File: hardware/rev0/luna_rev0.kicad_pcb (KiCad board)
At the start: 4 copper layers, 56 x 56 mm, 313 parts, among them IC1 ECP5-BGA256, J1 USB_C_Receptacle_USB2.0, J10 TC_SWD, J2 USB_C_Receptacle_USB2.0, J3 USB_A, J4 USB_C_Receptacle_USB2.0, J5 MEZZANINE, J6 MCU_SWD, J7 PMOD_A, J8 PMOD_B, Q1 PMOS, Q10 2PNP, Q11 2NPN, Q12 PMOS, Q13 2PNP, Q14 2PNP, Q15 2PNP, Q2 PMOS, Q3 2NPN, Q4 PMOS, Q5 PMOS, Q6 PMOS, Q7 PMOS, Q8 2NPN, Q9 PMOS, SW1 BTN_PROGRAM, SW2 BTN_RESET, SW3 BTN_USER, U1 PAC195X-1-WLCSP, U10 HyperRAM, U11 USB3343-CP, U12 FUSB302BMPX, U13 DPO2036, U14 DPO2036, U15 MIC5504-1.8YM5, U16 PI3USB102G, U2 FUSB302BMPX, U3 AP7361EA-33, U4 TCR2EF115, U5 MIC5504-2.5YM5, U6 ATSAMD11, U7 W25Q32JVSS, U8 USB3343-CP, U9 USB3343-CP, Y1 Osc60MHz

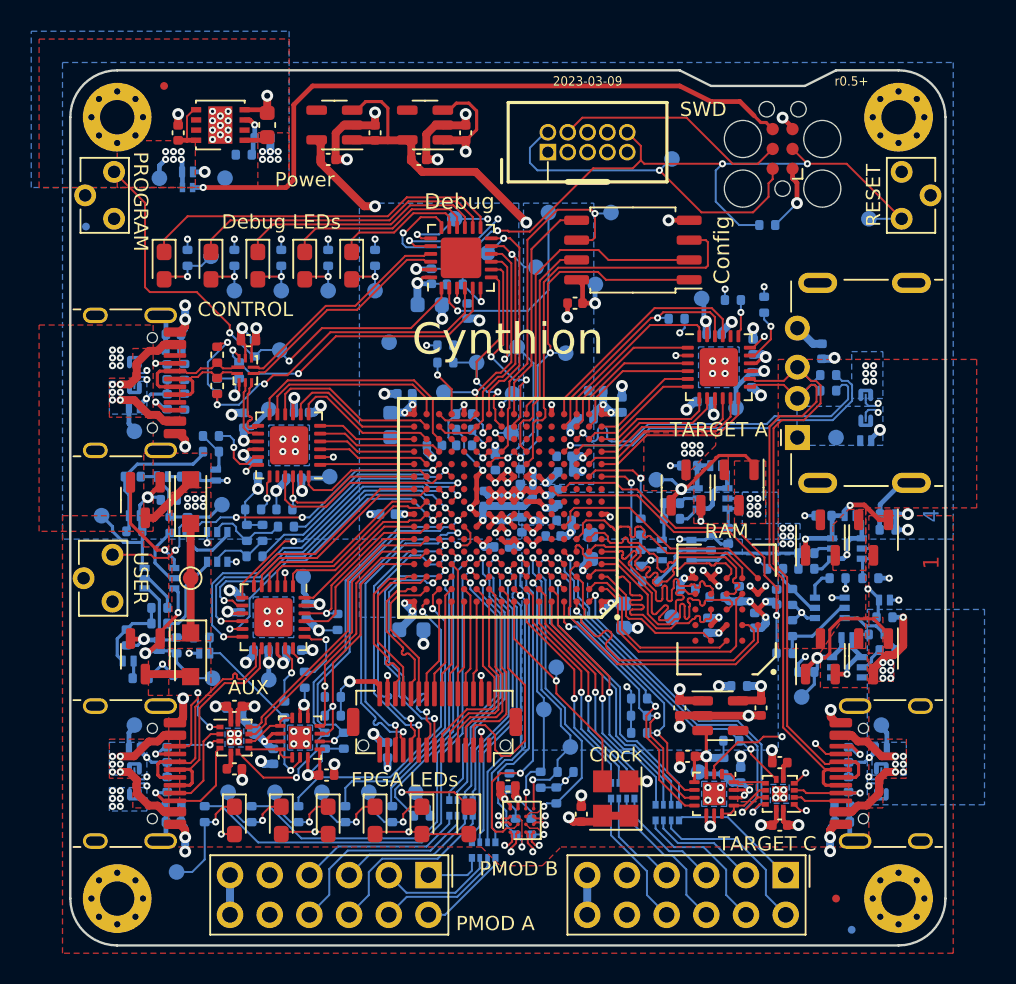
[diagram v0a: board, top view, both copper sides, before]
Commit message: Add additional silkscreen markings to front side.
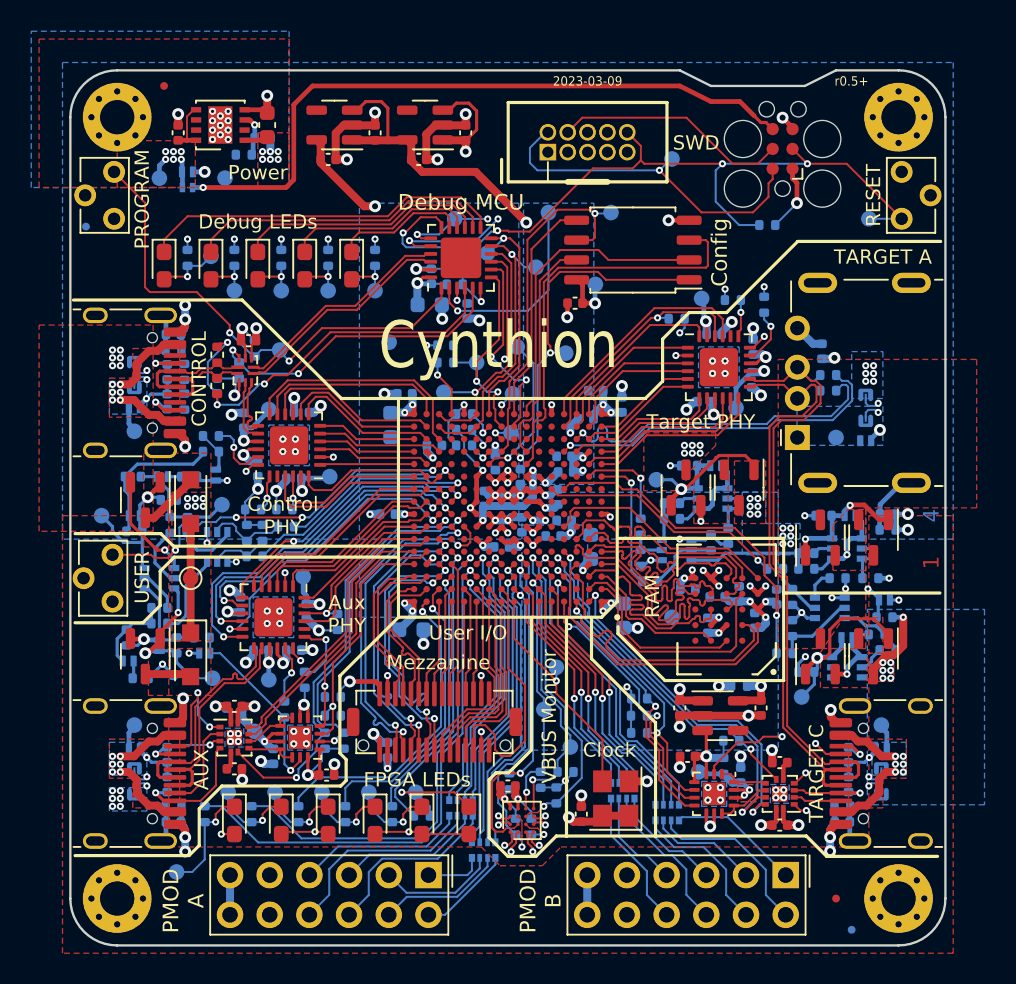
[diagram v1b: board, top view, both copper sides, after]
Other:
- board text added: "Aux PHY"
- board text added: "Control PHY"
- board text added: "Debug MCU"
- board text added: "Mezzanine"
- board text added: "Target PHY"
- board text added: "User I/O"
- board text added: "VBUS Monitor"
- board text removed: "Debug"
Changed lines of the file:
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@@
   (gr_line (start 108 70.9) (end 108.7 70.9) (layer "B.SilkS") (width 0.2032))
   (gr_line (start 136.223 102.2) (end 136.423 102) (layer "B.SilkS") (width 0.2032))
+  (gr_line (start 121.35 85) (end 125 85) (layer "F.SilkS") (width 0.2032))
+  (gr_line (start 143.6 79.5) (end 146 79.5) (layer "F.SilkS") (width 0.2032))
+  (gr_line (start 110.65 95.15) (end 125 95.15) (layer "F.SilkS") (width 0.2032))
+  (gr_line (start 149.65 103.05) (end 149.65 93.95) (layer "F.SilkS") (width 0.2032))
+  (gr_line (start 146 79.5) (end 150.55 74.95) (layer "F.SilkS") (width 0.2032))
+  (gr_line (start 133.5 107.5) (end 132.05 108.95) (layer "F.SilkS") (width 0.2032))
+  (gr_line (start 121.3 109.8) (end 113.7 109.8) (layer "F.SilkS") (width 0.2032))
+  (gr_line (start 110.6 94.45) (end 125 94.45) (layer "F.SilkS") (width 0.2032))
+  (gr_line (start 125 99) (end 121.25 102.75) (layer "F.SilkS") (width 0.2032))
+  (gr_line (start 132.05 108.95) (end 131.25 108.95) (layer "F.SilkS") (width 0.2032))
+  (gr_line (start 139.05 100.05) (end 139.05 99.6) (layer "F.SilkS") (width 0.2032))
+  (gr_line (start 104.3 99.35) (end 108.65 99.35) (layer "F.SilkS") (width 0.2032))
+  (gr_line (start 133.5 99) (end 133.5 107.5) (layer "F.SilkS") (width 0.2032))
+  (gr_line (start 133.8 114.3) (end 135.1 113) (layer "F.SilkS") (width 0.2032))
+  (gr_line (start 121.3 109.8) (end 121.65 109.45) (layer "F.SilkS") (width 0.2032))
+  (gr_line (start 141.9 83.9) (end 140.8 85) (layer "F.SilkS") (width 0.2032))
+  (gr_line (start 159.5 114.3) (end 152.4 114.3) (layer "F.SilkS") (width 0.2032))
+  (gr_line (start 115 78.7) (end 121.35 85) (layer "F.SilkS") (width 0.2032))
   (gr_line (start 131.6 71.2) (end 131.6 69.7) (layer "F.SilkS") (width 0.2032))
+  (gr_line (start 140.8 85) (end 139 85) (layer "F.SilkS") (width 0.2032))
+  (gr_line (start 112.25 111.25) (end 112.25 113.6) (layer "F.SilkS") (width 0.2032))
+  (gr_line (start 130.8 113.1) (end 132 114.3) (layer "F.SilkS") (width 0.2032))
+  (gr_line (start 108.65 99.35) (end 109.75 98.25) (layer "F.SilkS") (width 0.2032))
+  (gr_line (start 135.1 113) (end 135.75 113) (layer "F.SilkS") (width 0.2032))
+  (gr_line (start 109.75 96.05) (end 110.65 95.15) (layer "F.SilkS") (width 0.2032))
+  (gr_line (start 141.9 81.2) (end 141.9 83.9) (layer "F.SilkS") (width 0.2032))
+  (gr_line (start 149.65 93.95) (end 139.05 93.95) (layer "F.SilkS") (width 0.2032))
+  (gr_line (start 121.65 109.45) (end 121.65 108.1) (layer "F.SilkS") (width 0.2032))
+  (gr_line (start 139.05 100.05) (end 142.05 103.05) (layer "F.SilkS") (width 0.2032))
+  (gr_line (start 109.75 98.25) (end 109.75 96.05) (layer "F.SilkS") (width 0.2032))
+  (gr_line (start 111.6 114.25) (end 112.25 113.6) (layer "F.SilkS") (width 0.2032))
+  (gr_line (start 152.4 114.3) (end 151.1 113) (layer "F.SilkS") (width 0.2032))
+  (gr_line (start 104.3 93.65) (end 109.8 93.65) (layer "F.SilkS") (width 0.2032))
+  (gr_line (start 143.6 79.5) (end 141.9 81.2) (layer "F.SilkS") (width 0.2032))
+  (gr_line (start 137.35 101.65) (end 137.35 99) (layer "F.SilkS") (width 0.2032))
+  (gr_line (start 121.65 108.1) (end 121.25 107.7) (layer "F.SilkS") (width 0.2032))
+  (gr_line (start 109.8 93.65) (end 110.6 94.45) (layer "F.SilkS") (width 0.2032))
+  (gr_line (start 150.55 74.95) (end 159.7 74.95) (layer "F.SilkS") (width 0.2032))
+  (gr_line (start 132 114.3) (end 133.8 114.3) (layer "F.SilkS") (width 0.2032))
+  (gr_line (start 142.05 103.05) (end 149.65 103.05) (layer "F.SilkS") (width 0.2032))
+  (gr_line (start 121.25 107.7) (end 121.25 102.75) (layer "F.SilkS") (width 0.2032))
+  (gr_line (start 141.45 113.05) (end 141.45 105.75) (layer "F.SilkS") (width 0.2032))
+  (gr_line (start 149.65 97.45) (end 159.65 97.45) (layer "F.SilkS") (width 0.2032))
+  (gr_line (start 113.7 109.8) (end 112.25 111.25) (layer "F.SilkS") (width 0.2032))
+  (gr_line (start 104.2 78.7) (end 115 78.7) (layer "F.SilkS") (width 0.2032))
+  (gr_line (start 131.25 108.95) (end 130.8 109.4) (layer "F.SilkS") (width 0.2032))
+  (gr_line (start 135.75 113) (end 135.75 99) (layer "F.SilkS") (width 0.2032))
+  (gr_line (start 151.1 113) (end 135.75 113) (layer "F.SilkS") (width 0.2032))
+  (gr_line (start 130.8 109.4) (end 130.8 113.1) (layer "F.SilkS") (width 0.2032))
+  (gr_line (start 141.45 105.75) (end 137.35 101.65) (layer "F.SilkS") (width 0.2032))
+  (gr_line (start 111.6 114.25) (end 104.3 114.25) (layer "F.SilkS") (width 0.2032))
   (gr_circle (center 114.5 112) (end 115 112) (layer "Dwgs.User") (width 0.1) (fill none))
   (gr_line (start 148 109) (end 113 109) (layer "Dwgs.User") (width 0.2))
@@
     (effects (font (size 1 1) (thickness 0.15)) (justify mirror))
   )
-  (gr_text "Debug" (at 128.9 72.4) (layer "F.SilkS")
+  (gr_text "Debug MCU" (at 129 72.45) (layer "F.SilkS")
     (effects (font (size 1 1) (thickness 0.15)))
   )
-  (gr_text "Clock" (at 138.9 107.8) (layer "F.SilkS")
+  (gr_text "Clock" (at 138.5 107.5) (layer "F.SilkS")
     (effects (font (size 0.9144 0.9144) (thickness 0.15)))
   )
-  (gr_text "FPGA LEDs" (at 125.4 109.4) (layer "F.SilkS")
+  (gr_text "FPGA LEDs" (at 126.2 109.4) (layer "F.SilkS")
     (effects (font (size 0.9144 0.9238) (thickness 0.15)))
   )
@@
     (effects (font (size 0.6 0.5588) (thickness 0.125)))
   )
-  (gr_text "Debug LEDs" (at 117.5 73.7) (layer "F.SilkS")
+  (gr_text "Debug LEDs" (at 116 73.7) (layer "F.SilkS")
     (effects (font (size 0.9144 0.9144) (thickness 0.15)))
   )
-  (gr_text "SWD" (at 144.5 66.5) (layer "F.SilkS")
+  (gr_text "SWD" (at 144.05 68.65) (layer "F.SilkS")
     (effects (font (size 0.9144 0.9144) (thickness 0.15)))
   )
-  (gr_text "RAM" (at 146 93.5) (layer "F.SilkS")
+  (gr_text "PMOD\nA" (at 111.25 117.15 90) (layer "F.SilkS")
+    (effects (font (size 1 1) (thickness 0.15)))
+  )
+  (gr_text "RAM" (at 141.25 97.65 90) (layer "F.SilkS")
+    (effects (font (size 0.9144 0.9144) (thickness 0.15)))
+  )
+  (gr_text "USER" (at 108.6 96.45 90) (layer "F.SilkS")
     (effects (font (size 0.9144 0.9144) (thickness 0.15)))
   )
-  (gr_text "USER" (at 108.5 96.5 270) (layer "F.SilkS")
+  (gr_text "TARGET C" (at 151.75 109 90) (layer "F.SilkS")
     (effects (font (size 0.9144 0.9144) (thickness 0.15)))
   )
-  (gr_text "TARGET C" (at 148.6 113.5) (layer "F.SilkS")
+  (gr_text "PMOD\nB" (at 134.1 117.15 90) (layer "F.SilkS")
+    (effects (font (size 1 1) (thickness 0.15)))
+  )
+  (gr_text "Target PHY" (at 144.35 86.5) (layer "F.SilkS")
     (effects (font (size 0.9144 0.9144) (thickness 0.15)))
   )
-  (gr_text "Power" (at 119 71) (layer "F.SilkS")
+  (gr_text "Power" (at 116 70.55) (layer "F.SilkS")
     (effects (font (size 0.9144 0.9144) (thickness 0.15)))
   )
-  (gr_text "PMOD A" (at 131.2 118.6) (layer "F.SilkS")
+  (gr_text "VBUS Monitor" (at 134.65 105.35 90) (layer "F.SilkS")
     (effects (font (size 0.9144 0.9144) (thickness 0.15)))
   )
-  (gr_text "Config" (at 145.7 75.5 90) (layer "F.SilkS")
+  (gr_text "Config" (at 145.55 75.65 90) (layer "F.SilkS")
     (effects (font (size 1 1) (thickness 0.15)))
   )
+  (gr_text "User I/O" (at 129.45 100) (layer "F.SilkS")
+    (effects (font (size 0.9144 0.9144) (thickness 0.15)))
+  )
   (gr_text "RESET" (at 155.4 72 90) (layer "F.SilkS")
     (effects (font (size 0.9144 0.9144) (thickness 0.15)))
   )
-  (gr_text "PROGRAM" (at 108.5 72.4 270) (layer "F.SilkS")
+  (gr_text "PROGRAM" (at 108.6 72.25 90) (layer "F.SilkS")
+    (effects (font (size 0.9144 0.9144) (thickness 0.15)))
+  )
+  (gr_text "Mezzanine" (at 127.55 101.9) (layer "F.SilkS")
+    (effects (font (size 0.9144 0.9144) (thickness 0.15)))
+  )
+  (gr_text "Control\nPHY" (at 117.6 92.5) (layer "F.SilkS")
     (effects (font (size 0.9144 0.9144) (thickness 0.15)))
   )
-  (gr_text "PMOD B" (at 132.7 115.1) (layer "F.SilkS")
+  (gr_text "TARGET A" (at 156 75.95) (layer "F.SilkS")
     (effects (font (size 0.9144 0.9144) (thickness 0.15)))
   )
-  (gr_text "TARGET A" (at 145.5 87) (layer "F.SilkS")
+  (gr_text "CONTROL" (at 112.25 83.75 90) (layer "F.SilkS")
     (effects (font (size 0.9144 0.9144) (thickness 0.15)))
   )
-  (gr_text "CONTROL" (at 115.2 79.3) (layer "F.SilkS")
+  (gr_text "Aux\nPHY" (at 121.7 98.8) (layer "F.SilkS")
     (effects (font (size 0.9144 0.9144) (thickness 0.15)))
   )
-  (gr_text "AUX" (at 115.4 103.5) (layer "F.SilkS")
+  (gr_text "AUX" (at 112.4 108.75 90) (layer "F.SilkS")
     (effects (font (size 0.9144 0.9144) (thickness 0.15)))
   )
-  (gr_text "Cynthion" (at 132 81.2) (layer "F.SilkS")
-    (effects (font (size 2 2) (thickness 0.3)))
+  (gr_text "Cynthion" (at 131.4 81.6) (layer "F.SilkS")
+    (effects (font (size 3 2.5) (thickness 0.3)))
   )
   (gr_text "1.0 mm indent" (at 148 55) (layer "Dwgs.User")
@@
   (segment (start 131.44721 105.652) (end 131.9025 105.19671) (width 0.127) (layer "F.Cu") (net 348))
   (segment (start 129.3 106.04842) (end 129.69642 105.652) (width 0.127) (layer "F.Cu") (net 348))
-  (segment (start 131.6 102.21) (end 131.6 98) (width 0.127) (layer "F.Cu") (net 348))
+  (segment locked (start 131.6 102.21) (end 131.6 98) (width 0.127) (layer "F.Cu") (net 348))
   (segment (start 131.9025 102.5125) (end 131.9025 105.19671) (width 0.127) (layer "F.Cu") (net 348))
   (segment (start 131.9025 102.5125) (end 131.6 102.21) (width 0.127) (layer "F.Cu") (net 348))

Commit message: Second pass at silkscreen.
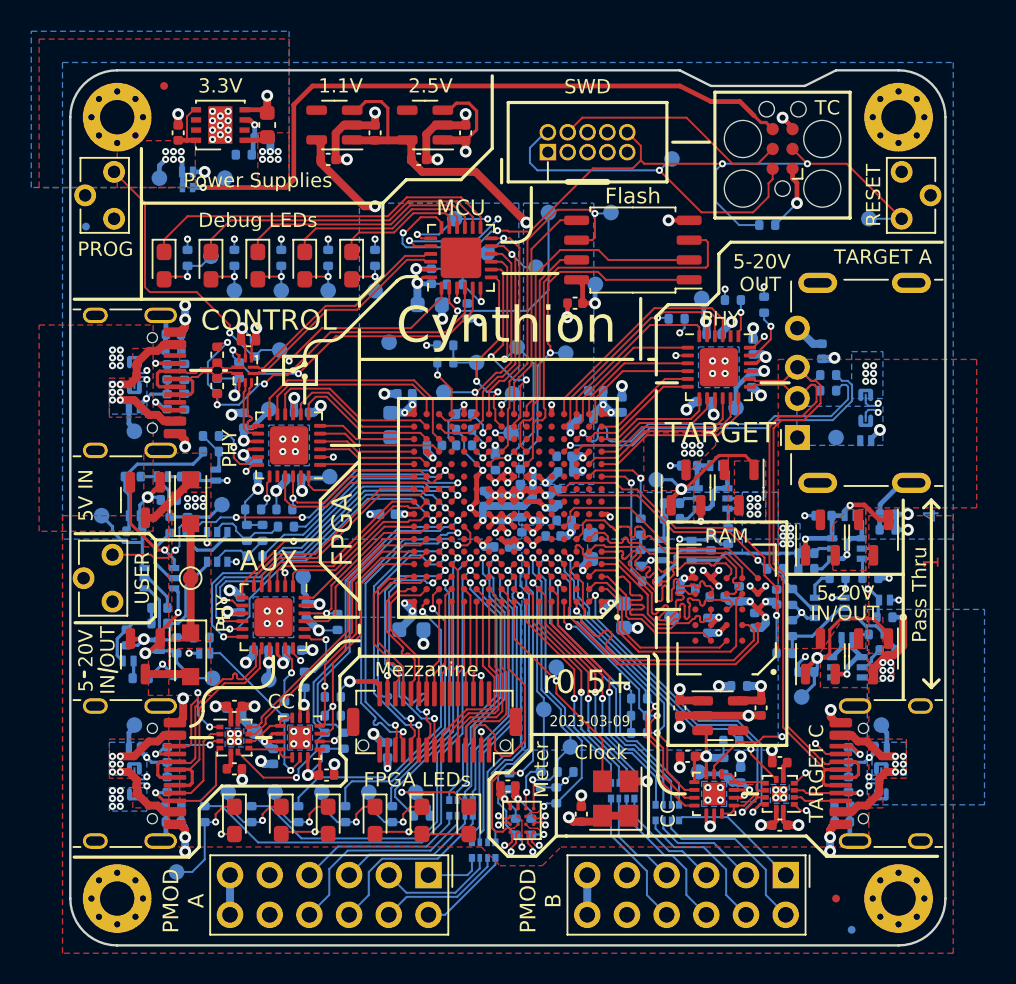
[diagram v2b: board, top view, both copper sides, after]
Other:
- board text added: "1.1V"
- board text added: "2.5V"
- board text added: "20V"
- board text added: "3.3V"
- board text added: "5"
- board text added: "5-20V"
- board text added: "5V IN"
- board text added: "CC"
- board text added: "FPGA"
- board text added: "Flash"
- board text added: "IN"
- board text added: "IN/OUT"
- board text added: "MCU"
- board text added: "Meter"
- board text added: "OUT"
- board text added: "PHY"
- board text added: "PROG"
- board text added: "Pass Thru"
- board text added: "Power Supplies"
- board text added: "TARGET"
- board text added: "TC"
- board text removed: "Aux PHY"
- board text removed: "Config"
- board text removed: "Control PHY"
- board text removed: "Debug MCU"
- board text removed: "PROGRAM"
- board text removed: "Power"
- board text removed: "Target PHY"
- board text removed: "User I/O"
- board text removed: "VBUS Monitor"
